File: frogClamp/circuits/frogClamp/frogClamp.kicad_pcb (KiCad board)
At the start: 2 copper layers, 13.5 x 4 mm, 17 parts, among them M1 Motor Pump, M2 Solenoid Valve, Q1 QM6006D, Q2 QM6006D, SW1 SW_SPDT

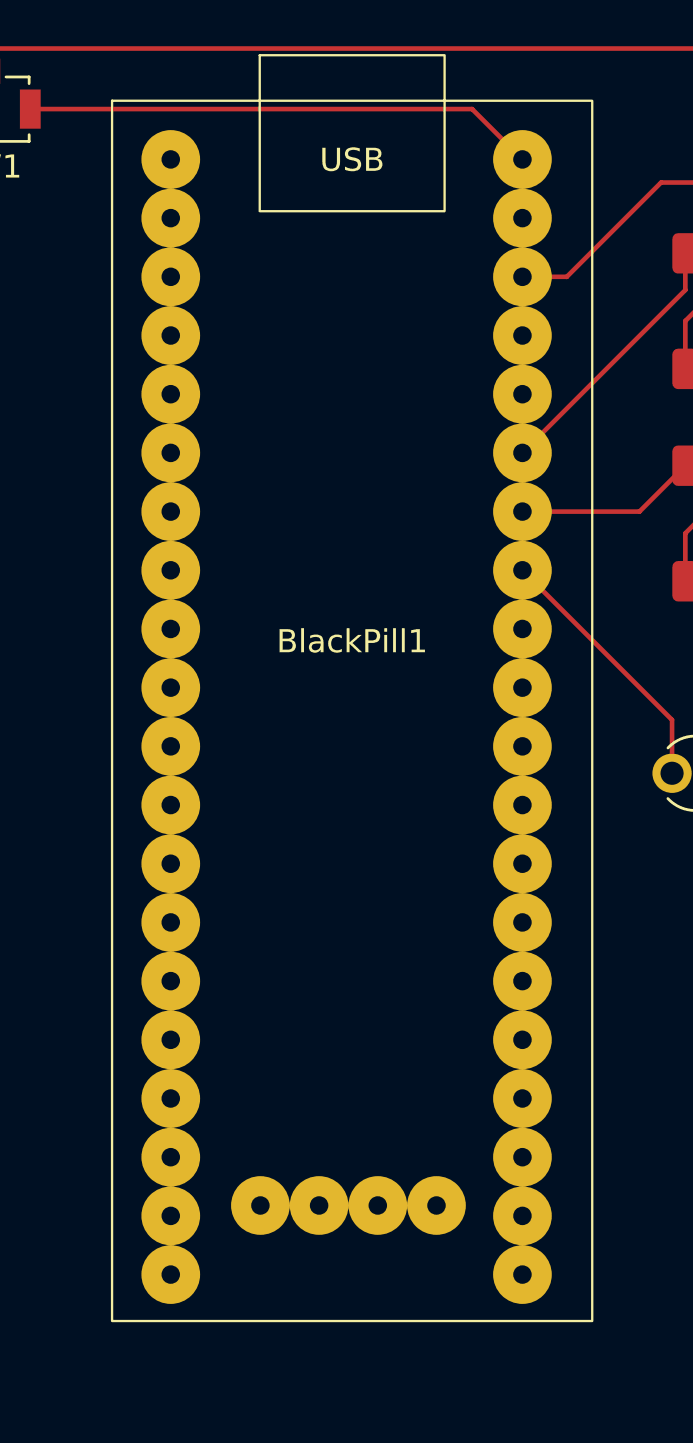
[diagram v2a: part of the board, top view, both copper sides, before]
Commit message: Updated parsing of footprints to include holes and 90 degree rotations.
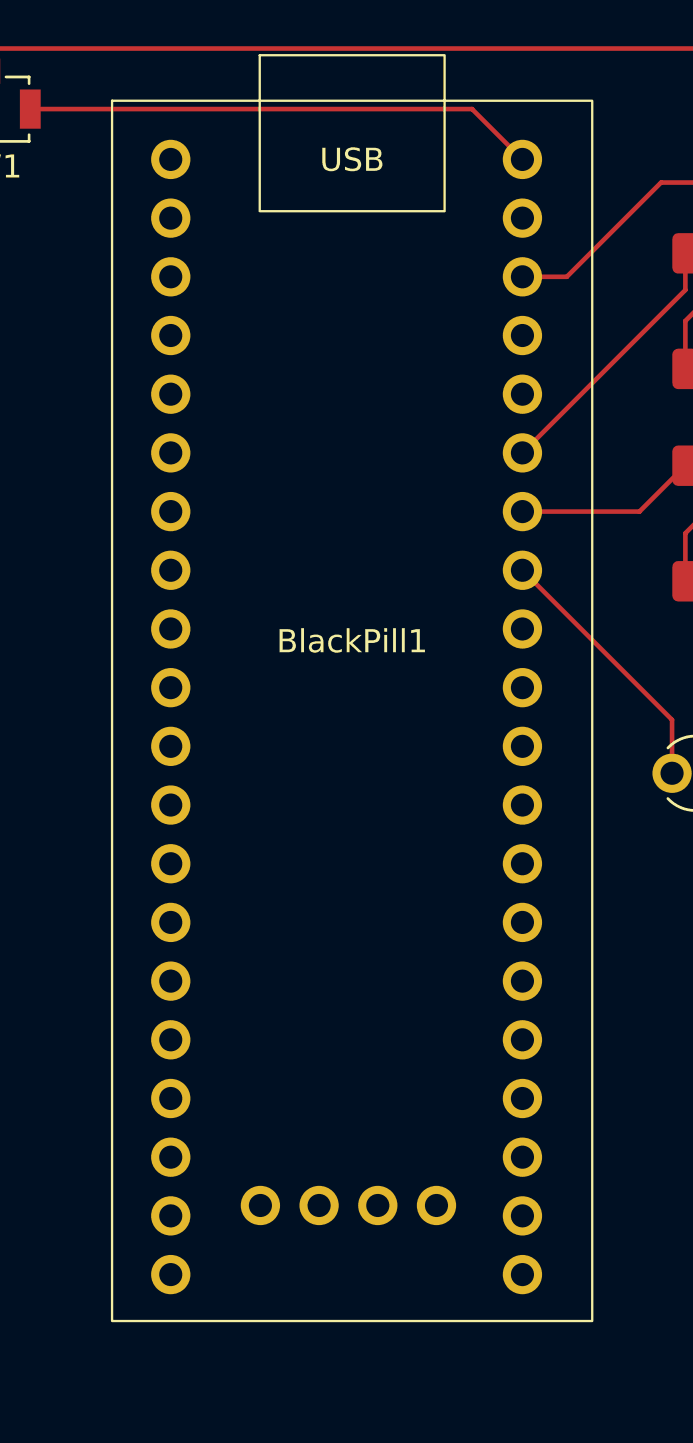
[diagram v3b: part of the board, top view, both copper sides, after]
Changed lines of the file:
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@@
 		(allow_soldermask_bridges_in_footprints no)
 		(tenting front back)
+		(aux_axis_origin 97.5 49.5)
 		(grid_origin 97.5 49.5)
 		(pcbplotparams
@@
 		(pad "1" thru_hole circle
 			(at -7.85 -23.865)
-			(size 2.54 2.54)
-			(drill 0.8)
+			(size 1.7 1.7)
+			(drill 1)
 			(layers "*.Cu" "*.Mask")
 			(remove_unused_layers no)
@@
 		(pad "2" thru_hole circle
 			(at -7.85 -21.325)
-			(size 2.54 2.54)
-			(drill 0.8)
+			(size 1.7 1.7)
+			(drill 1)
 			(layers "*.Cu" "*.Mask")
 			(remove_unused_layers no)
@@
 		(pad "3" thru_hole circle
 			(at -7.85 -18.785)
-			(size 2.54 2.54)
-			(drill 0.8)
+			(size 1.7 1.7)
+			(drill 1)
 			(layers "*.Cu" "*.Mask")
 			(remove_unused_layers no)
@@
 		(pad "4" thru_hole circle
 			(at -7.85 -16.245)
-			(size 2.54 2.54)
-			(drill 0.8)
+			(size 1.7 1.7)
+			(drill 1)
 			(layers "*.Cu" "*.Mask")
 			(remove_unused_layers no)
@@
 		(pad "5" thru_hole circle
 			(at -7.85 -13.705)
-			(size 2.54 2.54)
-			(drill 0.8)
+			(size 1.7 1.7)
+			(drill 1)
 			(layers "*.Cu" "*.Mask")
 			(remove_unused_layers no)
@@
 		(pad "6" thru_hole circle
 			(at -7.85 -11.165)
-			(size 2.54 2.54)
-			(drill 0.8)
+			(size 1.7 1.7)
+			(drill 1)
 			(layers "*.Cu" "*.Mask")
 			(remove_unused_layers no)
@@
 		(pad "7" thru_hole circle
 			(at -7.85 -8.625)
-			(size 2.54 2.54)
-			(drill 0.8)
+			(size 1.7 1.7)
+			(drill 1)
 			(layers "*.Cu" "*.Mask")
 			(remove_unused_layers no)
@@
 		(pad "8" thru_hole circle
 			(at -7.85 -6.085)
-			(size 2.54 2.54)
-			(drill 0.8)
+			(size 1.7 1.7)
+			(drill 1)
 			(layers "*.Cu" "*.Mask")
 			(remove_unused_layers no)
@@
 		(pad "9" thru_hole circle
 			(at -7.85 -3.545)
-			(size 2.54 2.54)
-			(drill 0.8)
+			(size 1.7 1.7)
+			(drill 1)
 			(layers "*.Cu" "*.Mask")
 			(remove_unused_layers no)
@@
 		(pad "10" thru_hole circle
 			(at -7.85 -1.005)
-			(size 2.54 2.54)
-			(drill 0.8)
+			(size 1.7 1.7)
+			(drill 1)
 			(layers "*.Cu" "*.Mask")
 			(remove_unused_layers no)
@@
 		(pad "11" thru_hole circle
 			(at -7.85 1.535)
-			(size 2.54 2.54)
-			(drill 0.8)
+			(size 1.7 1.7)
+			(drill 1)
 			(layers "*.Cu" "*.Mask")
 			(remove_unused_layers no)
@@
 		(pad "12" thru_hole circle
 			(at -7.85 4.075)
-			(size 2.54 2.54)
-			(drill 0.8)
+			(size 1.7 1.7)
+			(drill 1)
 			(layers "*.Cu" "*.Mask")
 			(remove_unused_layers no)
@@
 		(pad "13" thru_hole circle
 			(at -7.85 6.615)
-			(size 2.54 2.54)
-			(drill 0.8)
+			(size 1.7 1.7)
+			(drill 1)
 			(layers "*.Cu" "*.Mask")
 			(remove_unused_layers no)
@@
 		(pad "14" thru_hole circle
 			(at -7.85 9.155)
-			(size 2.54 2.54)
-			(drill 0.8)
+			(size 1.7 1.7)
+			(drill 1)
 			(layers "*.Cu" "*.Mask")
 			(remove_unused_layers no)
@@
 		(pad "15" thru_hole circle
 			(at -7.85 11.695)
-			(size 2.54 2.54)
-			(drill 0.8)
+			(size 1.7 1.7)
+			(drill 1)
 			(layers "*.Cu" "*.Mask")
 			(remove_unused_layers no)
@@
 		(pad "16" thru_hole circle
 			(at -7.85 14.235)
-			(size 2.54 2.54)
-			(drill 0.8)
+			(size 1.7 1.7)
+			(drill 1)
 			(layers "*.Cu" "*.Mask")
 			(remove_unused_layers no)
@@
 		(pad "17" thru_hole circle
 			(at -7.85 16.775)
-			(size 2.54 2.54)
-			(drill 0.8)
+			(size 1.7 1.7)
+			(drill 1)
 			(layers "*.Cu" "*.Mask")
 			(remove_unused_layers no)
@@
 		(pad "18" thru_hole circle
 			(at -7.85 19.315)
-			(size 2.54 2.54)
-			(drill 0.8)
+			(size 1.7 1.7)
+			(drill 1)
 			(layers "*.Cu" "*.Mask")
 			(remove_unused_layers no)
@@
 		(pad "19" thru_hole circle
 			(at -7.85 21.855)
-			(size 2.54 2.54)
-			(drill 0.8)
+			(size 1.7 1.7)
+			(drill 1)
 			(layers "*.Cu" "*.Mask")
 			(remove_unused_layers no)
@@
 		(pad "20" thru_hole circle
 			(at -7.85 24.395)
-			(size 2.54 2.54)
-			(drill 0.8)
+			(size 1.7 1.7)
+			(drill 1)
 			(layers "*.Cu" "*.Mask")
 			(remove_unused_layers no)
@@
 		(pad "21" thru_hole circle
 			(at 7.37 -23.865)
-			(size 2.54 2.54)
-			(drill 0.8)
+			(size 1.7 1.7)
+			(drill 1)
 			(layers "*.Cu" "*.Mask")
 			(remove_unused_layers no)
@@
 		(pad "22" thru_hole circle
 			(at 7.37 -21.325)
-			(size 2.54 2.54)
-			(drill 0.8)
+			(size 1.7 1.7)
+			(drill 1)
 			(layers "*.Cu" "*.Mask")
 			(remove_unused_layers no)
@@
 		(pad "23" thru_hole circle
 			(at 7.37 -18.785)
-			(size 2.54 2.54)
-			(drill 0.8)
+			(size 1.7 1.7)
+			(drill 1)
 			(layers "*.Cu" "*.Mask")
 			(remove_unused_layers no)
@@
 		(pad "24" thru_hole circle
 			(at 7.37 -16.245)
-			(size 2.54 2.54)
-			(drill 0.8)
+			(size 1.7 1.7)
+			(drill 1)
 			(layers "*.Cu" "*.Mask")
 			(remove_unused_layers no)
@@
 		(pad "25" thru_hole circle
 			(at 7.37 -13.705)
-			(size 2.54 2.54)
-			(drill 0.8)
+			(size 1.7 1.7)
+			(drill 1)
 			(layers "*.Cu" "*.Mask")
 			(remove_unused_layers no)
@@
 		(pad "26" thru_hole circle
 			(at 7.37 -11.165)
-			(size 2.54 2.54)
-			(drill 0.8)
+			(size 1.7 1.7)
+			(drill 1)
 			(layers "*.Cu" "*.Mask")
 			(remove_unused_layers no)
@@
 		(pad "27" thru_hole circle
 			(at 7.37 -8.625)
-			(size 2.54 2.54)
-			(drill 0.8)
+			(size 1.7 1.7)
+			(drill 1)
 			(layers "*.Cu" "*.Mask")
 			(remove_unused_layers no)
@@
 		(pad "28" thru_hole circle
 			(at 7.37 -6.085)
-			(size 2.54 2.54)
-			(drill 0.8)
+			(size 1.7 1.7)
+			(drill 1)
 			(layers "*.Cu" "*.Mask")
 			(remove_unused_layers no)
@@
 		(pad "29" thru_hole circle
 			(at 7.37 -3.545)
-			(size 2.54 2.54)
-			(drill 0.8)
+			(size 1.7 1.7)
+			(drill 1)
 			(layers "*.Cu" "*.Mask")
 			(remove_unused_layers no)
@@
 		(pad "30" thru_hole circle
 			(at 7.37 -1.005)
-			(size 2.54 2.54)
-			(drill 0.8)
+			(size 1.7 1.7)
+			(drill 1)
 			(layers "*.Cu" "*.Mask")
 			(remove_unused_layers no)
@@
 		(pad "31" thru_hole circle
 			(at 7.37 1.535)
-			(size 2.54 2.54)
-			(drill 0.8)
+			(size 1.7 1.7)
+			(drill 1)
 			(layers "*.Cu" "*.Mask")
 			(remove_unused_layers no)
@@
 		(pad "32" thru_hole circle
 			(at 7.37 4.075)
-			(size 2.54 2.54)
-			(drill 0.8)
+			(size 1.7 1.7)
+			(drill 1)
 			(layers "*.Cu" "*.Mask")
 			(remove_unused_layers no)
@@
 		(pad "33" thru_hole circle
 			(at 7.37 6.615)
-			(size 2.54 2.54)
-			(drill 0.8)
+			(size 1.7 1.7)
+			(drill 1)
 			(layers "*.Cu" "*.Mask")
 			(remove_unused_layers no)
@@
 		(pad "34" thru_hole circle
 			(at 7.37 9.155)
-			(size 2.54 2.54)
-			(drill 0.8)
+			(size 1.7 1.7)
+			(drill 1)
 			(layers "*.Cu" "*.Mask")
 			(remove_unused_layers no)
@@
 		(pad "35" thru_hole circle
 			(at 7.37 11.695)
-			(size 2.54 2.54)
-			(drill 0.8)
+			(size 1.7 1.7)
+			(drill 1)
 			(layers "*.Cu" "*.Mask")
 			(remove_unused_layers no)
@@
 		(pad "36" thru_hole circle
 			(at 7.37 14.235)
-			(size 2.54 2.54)
-			(drill 0.8)
+			(size 1.7 1.7)
+			(drill 1)
 			(layers "*.Cu" "*.Mask")
 			(remove_unused_layers no)
@@
 		(pad "37" thru_hole circle
 			(at 7.37 16.775)
-			(size 2.54 2.54)
-			(drill 0.8)
+			(size 1.7 1.7)
+			(drill 1)
 			(layers "*.Cu" "*.Mask")
 			(remove_unused_layers no)
@@
 		(pad "38" thru_hole circle
 			(at 7.37 19.315)
-			(size 2.54 2.54)
-			(drill 0.8)
+			(size 1.7 1.7)
+			(drill 1)
 			(layers "*.Cu" "*.Mask")
 			(remove_unused_layers no)
@@
 		(pad "39" thru_hole circle
 			(at 7.37 21.855)
-			(size 2.54 2.54)
-			(drill 0.8)
+			(size 1.7 1.7)
+			(drill 1)
 			(layers "*.Cu" "*.Mask")
 			(remove_unused_layers no)
@@
 		(pad "40" thru_hole circle
 			(at 7.37 24.395)
-			(size 2.54 2.54)
-			(drill 0.8)
+			(size 1.7 1.7)
+			(drill 1)
 			(layers "*.Cu" "*.Mask")
 			(remove_unused_layers no)
@@
 		(pad "41" thru_hole circle
 			(at -3.97 21.405)
-			(size 2.54 2.54)
-			(drill 0.8)
+			(size 1.7 1.7)
+			(drill 1)
 			(layers "*.Cu" "*.Mask")
 			(remove_unused_layers no)
@@
 		(pad "42" thru_hole circle
 			(at -1.43 21.405)
-			(size 2.54 2.54)
-			(drill 0.8)
+			(size 1.7 1.7)
+			(drill 1)
 			(layers "*.Cu" "*.Mask")
 			(remove_unused_layers no)
@@
 		(pad "43" thru_hole circle
 			(at 1.11 21.405)
-			(size 2.54 2.54)
-			(drill 0.8)
+			(size 1.7 1.7)
+			(drill 1)
 			(layers "*.Cu" "*.Mask")
 			(remove_unused_layers no)
@@
 		(pad "44" thru_hole circle
 			(at 3.65 21.405)
-			(size 2.54 2.54)
-			(drill 0.8)
-			(layers "*.Cu" "*.Mask")
-			(remove_unused_layers no)
+			(size 1.7 1.7)
+			(drill 1)
+			(layers "*.Cu" "*.Mask")
+			(remove_unused_layers no)
